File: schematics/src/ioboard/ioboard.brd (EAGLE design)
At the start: 81.3 x 99.1 mm, 72 parts, among them IC1 TL072P, IC2 TL072P, IC3 TL072P

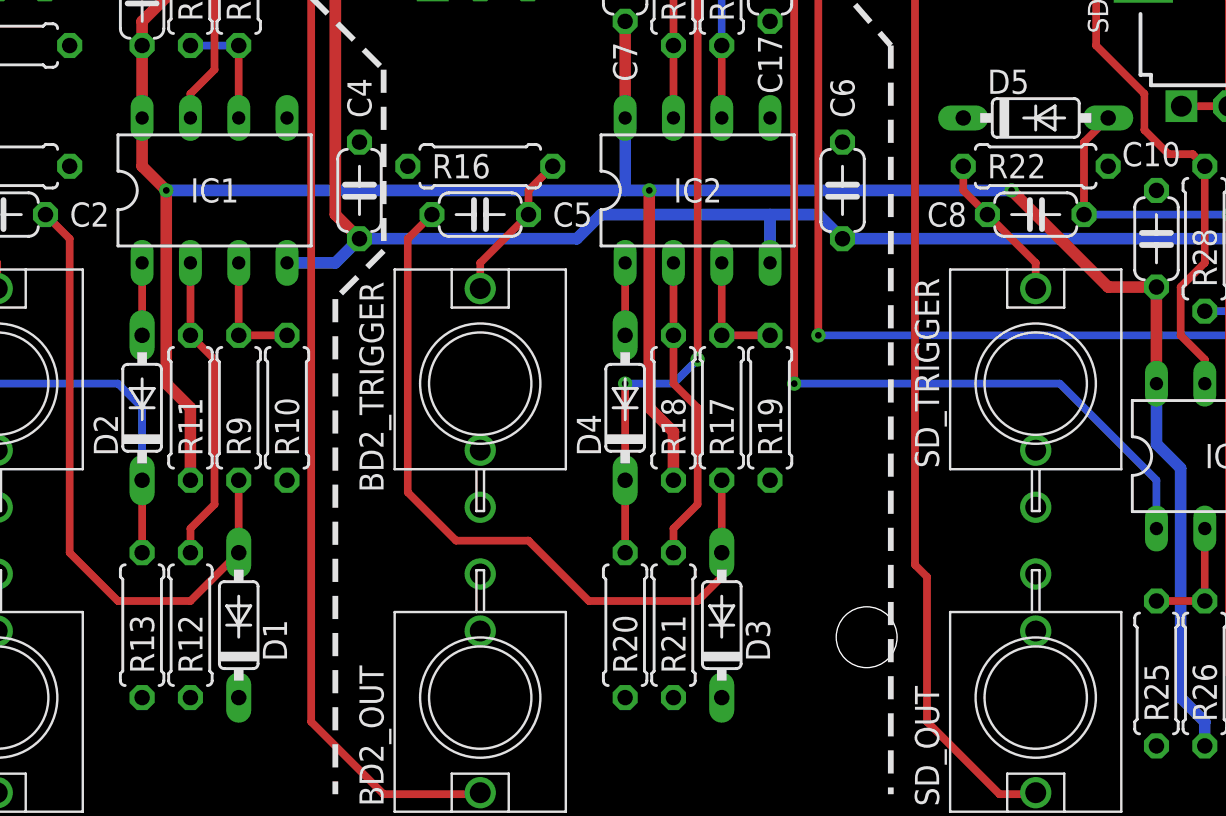
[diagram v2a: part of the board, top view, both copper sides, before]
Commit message: Fixed schematics & descriptions
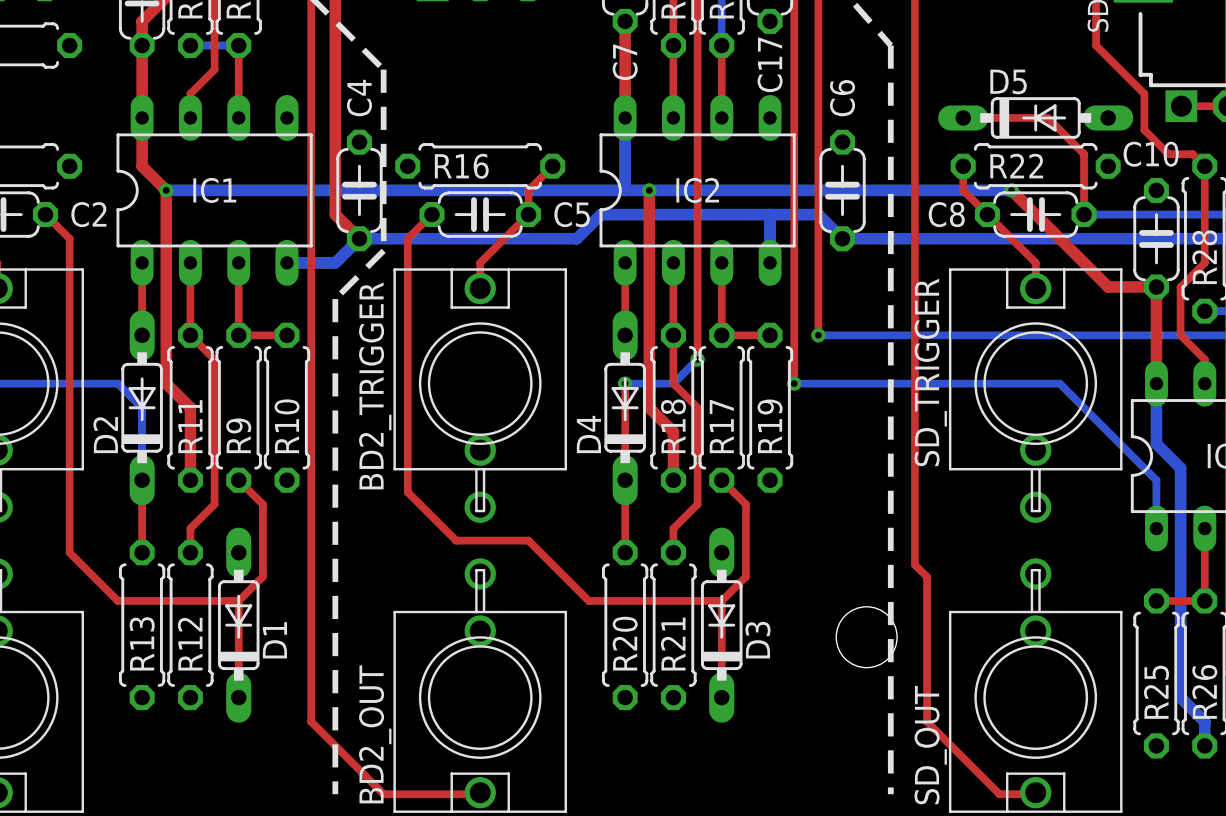
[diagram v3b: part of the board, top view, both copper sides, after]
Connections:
- net GND: now also D1.A, D3.A, D5.A; no longer D1.C, D3.C, D5.C
- net N$16: now also D3.C; no longer D3.A
- net N$22: now also D5.C; no longer D5.A
- net N$9: now also D1.C; no longer D1.A
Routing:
- net N$9: track 33.1 -> 40.7 mm
- net N$16: track 39.6 -> 46.5 mm
- net N$22: track 41.7 -> 46.4 mm
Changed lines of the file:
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@@
 <contactref element="IC1" pad="5"/>
 <contactref element="R8" pad="1"/>
-<contactref element="D1" pad="C"/>
 <contactref element="R10" pad="2"/>
 <contactref element="R12" pad="2"/>
@@
 <contactref element="R19" pad="2"/>
 <contactref element="R16" pad="1"/>
-<contactref element="D3" pad="C"/>
 <contactref element="R20" pad="2"/>
 <contactref element="BD2_TRIGGER" pad="P$3"/>
@@
 <contactref element="SD_TRIGGER" pad="P$3"/>
 <contactref element="R22" pad="1"/>
-<contactref element="D5" pad="C"/>
 <contactref element="R24" pad="2"/>
 <contactref element="R25" pad="2"/>
@@
 <via x="74.295" y="79.375" extent="1-16" drill="0.35"/>
 <via x="62.865" y="62.865" extent="1-16" drill="0.35"/>
+<contactref element="D3" pad="A"/>
+<contactref element="D5" pad="A"/>
+<contactref element="D1" pad="A"/>
+<wire x1="74.295" y1="79.375" x2="63.54" y2="89.52" width="0" layer="19" extent="1-1"/>
+<wire x1="62.865" y1="62.865" x2="74.295" y2="79.375" width="0" layer="19" extent="1-1"/>
+<wire x1="57.15" y1="63.5" x2="62.865" y2="62.865" width="0" layer="19" extent="1-1"/>
+<wire x1="77.47" y1="54.61" x2="62.865" y2="62.865" width="0" layer="19" extent="1-1"/>
+<wire x1="78.74" y1="51.435" x2="77.47" y2="54.61" width="0" layer="19" extent="1-1"/>
+<wire x1="68.58" y1="36.83" x2="78.74" y2="51.435" width="0" layer="19" extent="1-1"/>
+<wire x1="68.58" y1="34.29" x2="68.58" y2="36.83" width="0" layer="19" extent="1-1"/>
+<wire x1="71.12" y1="33.02" x2="68.58" y2="34.29" width="0" layer="19" extent="1-1"/>
+<wire x1="78.74" y1="33.02" x2="71.12" y2="33.02" width="0" layer="19" extent="1-1"/>
+<wire x1="78.74" y1="22.86" x2="78.74" y2="33.02" width="0" layer="19" extent="1-1"/>
+<wire x1="54.61" y1="35.56" x2="68.58" y2="36.83" width="0" layer="19" extent="1-1"/>
+<wire x1="50.8" y1="36.83" x2="54.61" y2="35.56" width="0" layer="19" extent="1-1"/>
+<wire x1="50.8" y1="41.91" x2="50.8" y2="36.83" width="0" layer="19" extent="1-1"/>
+<wire x1="43.18" y1="46.99" x2="50.8" y2="41.91" width="0" layer="19" extent="1-1"/>
+<wire x1="64.77" y1="16.36" x2="78.74" y2="22.86" width="0" layer="19" extent="1-1"/>
+<wire x1="64.77" y1="12.85" x2="64.77" y2="16.36" width="0" layer="19" extent="1-1"/>
+<wire x1="71.12" y1="3.81" x2="64.77" y2="12.85" width="0" layer="19" extent="1-1"/>
+<wire x1="78.74" y1="3.81" x2="71.12" y2="3.81" width="0" layer="19" extent="1-1"/>
+<wire x1="50.8" y1="17.78" x2="64.77" y2="16.36" width="0" layer="19" extent="1-1"/>
+<wire x1="48.26" y1="13.97" x2="50.8" y2="17.78" width="0" layer="19" extent="1-1"/>
+<wire x1="45.72" y1="6.35" x2="48.26" y2="13.97" width="0" layer="19" extent="1-1"/>
+<wire x1="43.18" y1="6.35" x2="45.72" y2="6.35" width="0" layer="19" extent="1-1"/>
+<wire x1="35.56" y1="12.85" x2="43.18" y2="6.35" width="0" layer="19" extent="1-1"/>
+<wire x1="35.56" y1="16.36" x2="35.56" y2="12.85" width="0" layer="19" extent="1-1"/>
+<wire x1="25.4" y1="17.78" x2="35.56" y2="16.36" width="0" layer="19" extent="1-1"/>
+<wire x1="22.86" y1="13.97" x2="25.4" y2="17.78" width="0" layer="19" extent="1-1"/>
+<wire x1="20.32" y1="6.35" x2="22.86" y2="13.97" width="0" layer="19" extent="1-1"/>
+<wire x1="17.78" y1="6.35" x2="20.32" y2="6.35" width="0" layer="19" extent="1-1"/>
+<wire x1="10.16" y1="12.85" x2="17.78" y2="6.35" width="0" layer="19" extent="1-1"/>
+<wire x1="10.16" y1="16.36" x2="10.16" y2="12.85" width="0" layer="19" extent="1-1"/>
+<wire x1="31.75" y1="34.29" x2="43.18" y2="46.99" width="0" layer="19" extent="1-1"/>
+<wire x1="29.21" y1="35.56" x2="31.75" y2="34.29" width="0" layer="19" extent="1-1"/>
+<wire x1="25.4" y1="36.83" x2="29.21" y2="35.56" width="0" layer="19" extent="1-1"/>
+<wire x1="17.78" y1="45.72" x2="25.4" y2="36.83" width="0" layer="19" extent="1-1"/>
+<wire x1="13.97" y1="40.64" x2="17.78" y2="45.72" width="0" layer="19" extent="1-1"/>
+<wire x1="13.97" y1="34.29" x2="13.97" y2="40.64" width="0" layer="19" extent="1-1"/>
+<wire x1="33.06" y1="89.52" x2="63.54" y2="89.52" width="0" layer="19" extent="1-1"/>
+<wire x1="22.86" y1="82.55" x2="33.06" y2="89.52" width="0" layer="19" extent="1-1"/>
+<wire x1="7.66" y1="89.52" x2="22.86" y2="82.55" width="0" layer="19" extent="1-1"/>
+<wire x1="2.54" y1="92.71" x2="7.66" y2="89.52" width="0" layer="19" extent="1-1"/>
 </signal>
 <signal name="BD1_TUNE_A">
@@
 <signal name="N$9">
 <contactref element="C2" pad="2"/>
-<contactref element="D1" pad="A"/>
 <contactref element="R9" pad="2"/>
-<wire x1="22.86" y1="13.97" x2="22.86" y2="17.78" width="0.4064" layer="1"/>
 <wire x1="12.7" y1="31.75" x2="13.97" y2="30.48" width="0.4064" layer="1"/>
 <wire x1="13.97" y1="13.97" x2="16.51" y2="11.43" width="0.4064" layer="1"/>
-<wire x1="16.51" y1="11.43" x2="20.32" y2="11.43" width="0.4064" layer="1"/>
-<wire x1="20.32" y1="11.43" x2="22.86" y2="13.97" width="0.4064" layer="1"/>
 <wire x1="13.97" y1="30.48" x2="13.97" y2="13.97" width="0.4064" layer="1"/>
+<contactref element="D1" pad="C"/>
+<wire x1="22.86" y1="11.43" x2="22.86" y2="6.35" width="0.4064" layer="1"/>
+<wire x1="16.51" y1="11.43" x2="22.86" y2="11.43" width="0.4064" layer="1"/>
+<wire x1="22.86" y1="17.78" x2="24.13" y2="16.51" width="0.4064" layer="1"/>
+<wire x1="24.13" y1="16.51" x2="24.13" y2="12.7" width="0.4064" layer="1"/>
+<wire x1="24.13" y1="12.7" x2="22.86" y2="11.43" width="0.4064" layer="1"/>
 </signal>
 <signal name="N$10">
@@
 <contactref element="C5" pad="2"/>
 <contactref element="R17" pad="2"/>
-<contactref element="D3" pad="A"/>
-<wire x1="46.99" y1="11.43" x2="41.275" y2="11.43" width="0.4064" layer="1"/>
+<wire x1="48.26" y1="11.43" x2="41.275" y2="11.43" width="0.4064" layer="1"/>
 <wire x1="41.275" y1="11.43" x2="38.1" y2="14.605" width="0.4064" layer="1"/>
 <wire x1="38.1" y1="14.605" x2="34.29" y2="14.605" width="0.4064" layer="1"/>
@@
 <wire x1="31.75" y1="30.48" x2="33.02" y2="31.75" width="0.4064" layer="1"/>
 <wire x1="34.29" y1="14.605" x2="31.75" y2="17.145" width="0.4064" layer="1"/>
-<wire x1="48.26" y1="17.78" x2="48.26" y2="13.97" width="0.4064" layer="1"/>
-<wire x1="48.26" y1="13.97" x2="48.26" y2="12.7" width="0.4064" layer="1"/>
-<wire x1="48.26" y1="12.7" x2="46.99" y2="11.43" width="0.4064" layer="1"/>
+<contactref element="D3" pad="C"/>
+<wire x1="48.26" y1="6.35" x2="48.26" y2="11.43" width="0.4064" layer="1"/>
+<wire x1="48.26" y1="17.78" x2="49.53" y2="16.51" width="0.4064" layer="1"/>
+<wire x1="49.53" y1="16.51" x2="49.53" y2="12.7" width="0.4064" layer="1"/>
+<wire x1="49.53" y1="12.7" x2="48.26" y2="11.43" width="0.4064" layer="1"/>
 </signal>
 <signal name="N$17">
@@
 <contactref element="C8" pad="2"/>
 <contactref element="R23" pad="2"/>
-<contactref element="D5" pad="A"/>
-<wire x1="68.58" y1="36.83" x2="67.31" y2="35.56" width="0.4064" layer="1"/>
-<wire x1="67.31" y1="35.56" x2="67.31" y2="31.75" width="0.4064" layer="1"/>
+<wire x1="67.31" y1="34.925" x2="67.31" y2="31.75" width="0.4064" layer="1"/>
 <wire x1="67.31" y1="31.75" x2="74.93" y2="31.75" width="0.4064" layer="16"/>
 <via x="74.93" y="31.75" extent="1-16" drill="0.35"/>
@@
 <wire x1="74.93" y1="7.62" x2="76.2" y2="6.35" width="0.4064" layer="1"/>
 <wire x1="76.2" y1="6.35" x2="76.2" y2="3.81" width="0.4064" layer="1"/>
+<contactref element="D5" pad="C"/>
+<wire x1="60.96" y1="36.83" x2="65.405" y2="36.83" width="0.4064" layer="1"/>
+<wire x1="65.405" y1="36.83" x2="67.31" y2="34.925" width="0.4064" layer="1"/>
 </signal>
 <signal name="N$23">

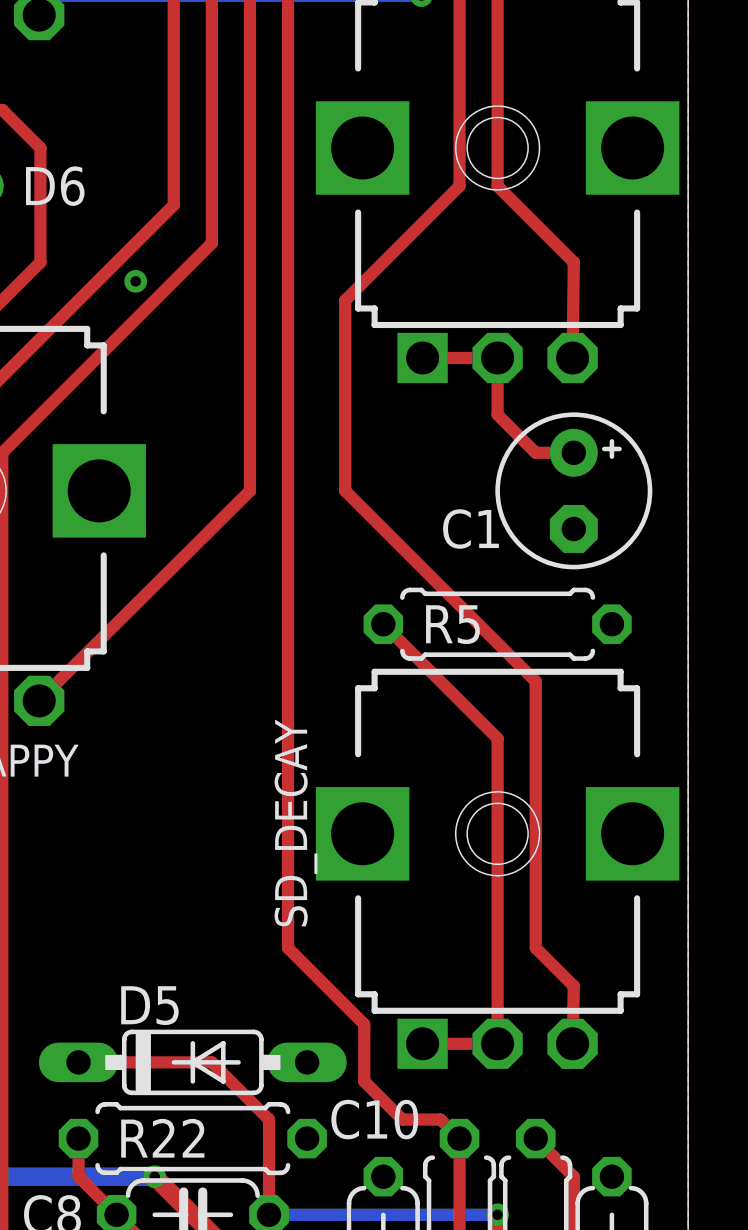
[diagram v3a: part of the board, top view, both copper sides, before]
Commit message: Fixed orentation SD Decay pot
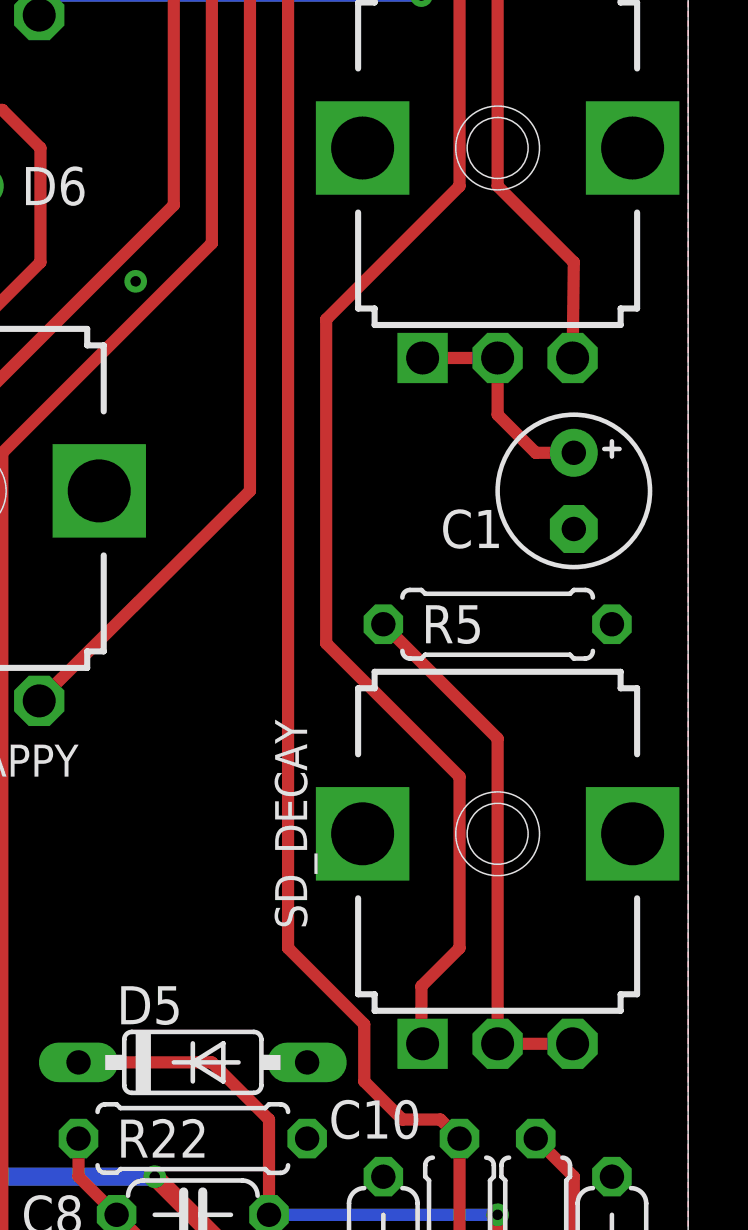
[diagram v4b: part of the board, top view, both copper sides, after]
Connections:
- net N$7: now also SD_DECAY.3; no longer SD_DECAY.1
- net SD_DECAY_A: now also SD_DECAY.1; no longer SD_DECAY.3
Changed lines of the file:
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@@
 </signal>
 <signal name="SD_DECAY_A">
-<contactref element="SD_DECAY" pad="3"/>
 <contactref element="SD_CON" pad="6"/>
 <wire x1="78.74" y1="78.74" x2="76.2" y2="78.74" width="0.4064" layer="1"/>
 <wire x1="76.2" y1="78.74" x2="73.66" y2="76.2" width="0.4064" layer="1"/>
-<wire x1="73.66" y1="66.04" x2="69.85" y2="62.23" width="0.4064" layer="1"/>
-<wire x1="69.85" y1="62.23" x2="69.85" y2="55.88" width="0.4064" layer="1"/>
-<wire x1="69.85" y1="55.88" x2="76.2" y2="49.53" width="0.4064" layer="1"/>
-<wire x1="76.2" y1="49.53" x2="76.2" y2="40.64" width="0.4064" layer="1"/>
-<wire x1="76.2" y1="40.64" x2="77.47" y2="39.37" width="0.4064" layer="1"/>
-<wire x1="77.47" y1="39.37" x2="77.43" y2="37.45" width="0.4064" layer="1"/>
+<wire x1="73.66" y1="66.04" x2="69.215" y2="61.595" width="0.4064" layer="1"/>
+<wire x1="69.215" y1="61.595" x2="69.215" y2="50.8" width="0.4064" layer="1"/>
+<wire x1="69.215" y1="50.8" x2="73.66" y2="46.355" width="0.4064" layer="1"/>
+<wire x1="73.66" y1="46.355" x2="73.66" y2="40.64" width="0.4064" layer="1"/>
+<wire x1="72.39" y1="39.37" x2="73.66" y2="40.64" width="0.4064" layer="1"/>
 <wire x1="73.66" y1="76.2" x2="73.66" y2="66.04" width="0.4064" layer="1"/>
+<contactref element="SD_DECAY" pad="1"/>
+<wire x1="72.43" y1="37.45" x2="72.39" y2="37.45" width="0.4064" layer="1"/>
+<wire x1="72.39" y1="37.45" x2="72.39" y2="39.37" width="0.4064" layer="1"/>
 </signal>
 <signal name="N$7">
-<contactref element="SD_DECAY" pad="1"/>
+<contactref element="R5" pad="2"/>
+<wire x1="71.12" y1="51.435" x2="74.93" y2="47.625" width="0.4064" layer="1"/>
+<contactref element="SD_DECAY" pad="3"/>
 <contactref element="SD_DECAY" pad="2"/>
-<contactref element="R5" pad="2"/>
-<wire x1="72.43" y1="37.45" x2="74.93" y2="37.45" width="0.4064" layer="1"/>
-<wire x1="71.12" y1="51.435" x2="74.93" y2="47.625" width="0.4064" layer="1"/>
 <wire x1="74.93" y1="47.625" x2="74.93" y2="37.45" width="0.4064" layer="1"/>
+<wire x1="74.93" y1="37.45" x2="77.43" y2="37.45" width="0.4064" layer="1"/>
 </signal>
 <signal name="N$6">
